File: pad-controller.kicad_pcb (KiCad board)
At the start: 2 copper layers, 86 x 64 mm, 50 parts, among them J4 Conn_01x02, J6 Conn_01x06, M1 Motor_Servo, M2 Motor_Servo, M3 Motor_Servo, M4 Motor_Servo, Q2 FQP30N06L, SW1 SW_Push_Dual, U1 Xbee, U2 TPS56121, U3 LD1117S33TR_SOT223

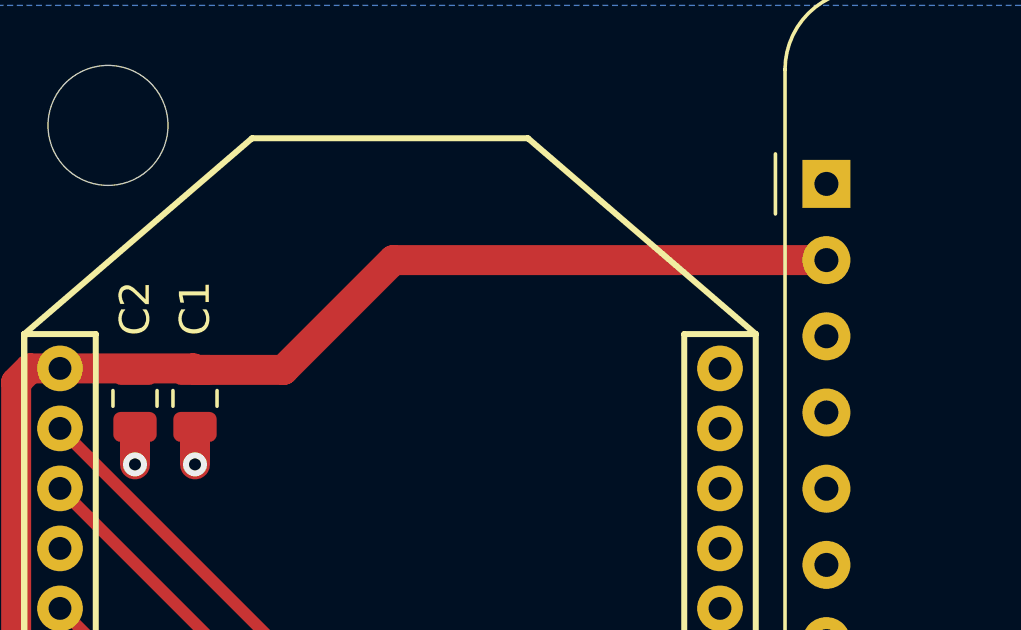
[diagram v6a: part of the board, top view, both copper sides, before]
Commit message: Adjust buck converter thermal vias
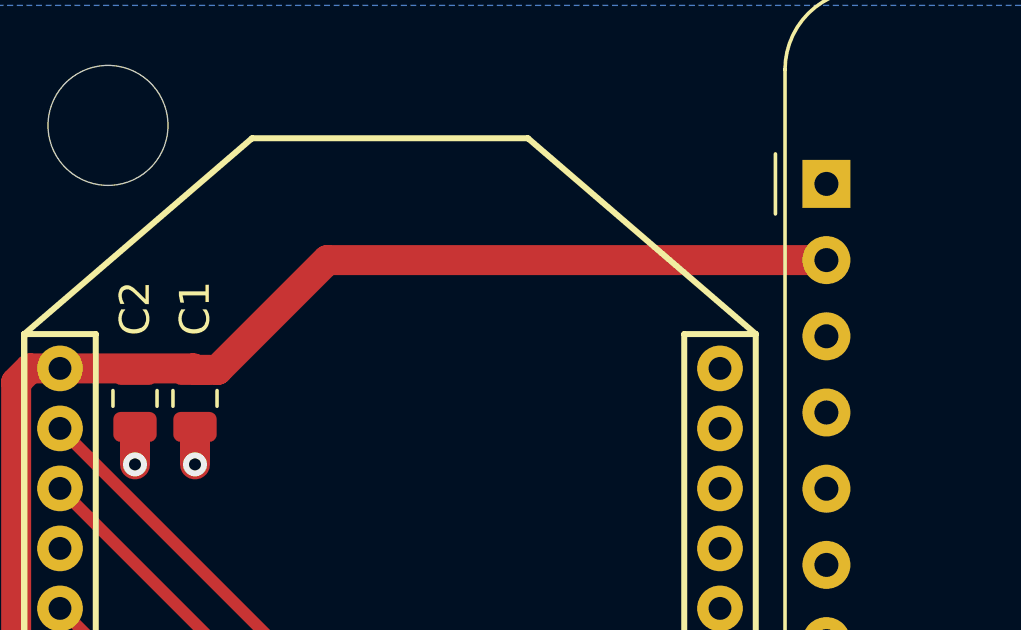
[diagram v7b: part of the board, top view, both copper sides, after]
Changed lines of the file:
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@@
       (net 35 "+BATT") (pintype "unspecified"))
     (pad "2" thru_hole circle (at 7.2 0 90) (size 6 6) (drill 4.5) (layers "*.Cu" "*.Mask")
-      (net 4 "GND") (pintype "unspecified"))
+      (net 4 "GND") (pintype "unspecified") (zone_connect 1) (thermal_bridge_width 2) (thermal_gap 0.5))
     (model "${KICAD6_3DMODEL_DIR}/Connector_AMASS.3dshapes/AMASS_XT60-M_1x02_P7.2mm_Vertical.wrl"
       (offset (xyz 0 0 0))
@@
     (tags "CMS SOT")
     (property "Description" "")
-    (property "Part No." "")
+    (property "Part No." "LD1117S33TR")
     (property "Sheetfile" "Power.kicad_sch")
     (property "Sheetname" "Power")
@@
     (property "Sheetfile" "pad-controller.kicad_sch")
     (property "Sheetname" "")
-    (property "ki_description" "Jumper, 2-pole, open")
-    (property "ki_keywords" "Jumper SPST")
+    (property "ki_description" "Solder Jumper, 2-pole, open")
+    (property "ki_keywords" "solder jumper SPST")
     (attr exclude_from_pos_files)
     (fp_text reference "JP2" (at 0 1.8) (layer "B.SilkS")
@@
     (effects (font (size 1 1) (thickness 0.15)) (justify right))
   )
-  (segment (start 114.51 69.49) (end 128.9475 69.49) (width 1) (layer "F.Cu") (net 2))
   (segment (start 107.85 73.1) (end 107.9 73.15) (width 1) (layer "F.Cu") (net 2))
   (segment (start 125.575 119.925) (end 125.575 120.925) (width 1) (layer "F.Cu") (net 2))
   (segment (start 103.4 73.1) (end 107.85 73.1) (width 1) (layer "F.Cu") (net 2))
   (segment (start 114.225 114.625) (end 101.938 102.338) (width 1) (layer "F.Cu") (net 2))
-  (segment (start 110.85 73.15) (end 114.51 69.49) (width 1) (layer "F.Cu") (net 2))
+  (segment (start 112.31 69.49) (end 128.9475 69.49) (width 1) (layer "F.Cu") (net 2))
   (segment (start 125.575 115.625) (end 125.575 114.625) (width 1) (layer "F.Cu") (net 2))
+  (segment (start 108.65 73.15) (end 112.31 69.49) (width 1) (layer "F.Cu") (net 2))
+  (segment (start 107.9 73.15) (end 108.65 73.15) (width 1) (layer "F.Cu") (net 2))
   (segment (start 102.4 73.1) (end 103.4 73.1) (width 1) (layer "F.Cu") (net 2))
   (segment (start 120.625 117.775) (end 123.425 117.775) (width 1) (layer "F.Cu") (net 2))
   (segment (start 125.575 114.625) (end 114.225 114.625) (width 1) (layer "F.Cu") (net 2))
-  (segment (start 107.9 73.15) (end 110.85 73.15) (width 1) (layer "F.Cu") (net 2))
   (segment (start 101.938 102.338) (end 101.938 73.562) (width 1) (layer "F.Cu") (net 2))
   (segment (start 123.425 117.775) (end 125.575 115.625) (width 1) (layer "F.Cu") (net 2))
